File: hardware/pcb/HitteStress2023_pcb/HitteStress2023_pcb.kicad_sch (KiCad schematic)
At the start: 5 parts

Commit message: Update drawing
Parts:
- added J1: Conn_01x02_Socket, Connector_Phoenix_GMSTB:PhoenixContact_GMSTBVA_2,5_2-G-7,62_1x02_P7.62mm_Vertical, symbol Connector:Conn_01x02_Socket
- added J2: Conn_01x02_Socket, my-KiCad-library:TerminalBlock_Phoenix_MPT-0,5-2-2.54_1x02_P2.54mm_Horizontal, symbol Connector:Conn_01x02_Socket
- P1: footprint (none) -> my-KiCad-library:HLK-5M05
- S1: value ~ -> AM2315C; footprint (none) -> my-KiCad-library:AM2315C
- S2: value ~ -> SPS30; footprint (none) -> my-KiCad-library:SPS30
- U1: renamed from U2; value ~ -> MINIDCDCBOOST5V; footprint (none) -> my-KiCad-library:MINIDCDCBOOST5V
- U2: renamed from U1; value ~ -> TTGO_T-Beam_T22_V1.1; footprint (none) -> my-KiCad-library:TTGO_T-Beam_T22_V1.1
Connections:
- net GND: now also P1.3 (-Vo), J2.1 (Pin_1)
- net at P1.1 (AC): now also J1.2 (Pin_2)
- net at P1.2 (AC): now also J1.1 (Pin_1)
- net 5V_I: now reaches P1.4 (+Vo)
- net 5V_I: now also J2.2 (Pin_2)
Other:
- moved on the sheet: U1
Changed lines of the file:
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@@
 (kicad_sch (version 20230121) (generator eeschema)
   (paper "A4")
+  (wire (pts (xy 81.28 64.77) (xy 81.28 66.04))
+    (stroke (width 0) (type default))
+  )
   (wire (pts (xy 177.8 64.77) (xy 193.04 64.77))
     (stroke (width 0) (type default))
   )
+  (wire (pts (xy 81.28 60.96) (xy 81.28 62.23))
+    (stroke (width 0) (type default))
+  )
+  (wire (pts (xy 44.45 66.04) (xy 44.45 64.77))
+    (stroke (width 0) (type default))
+  )
   (wire (pts (xy 177.8 97.79) (xy 193.04 97.79))
     (stroke (width 0) (type default))
@@
     (stroke (width 0) (type default))
   )
+  (wire (pts (xy 86.36 64.77) (xy 81.28 64.77))
+    (stroke (width 0) (type default))
+  )
+  (wire (pts (xy 36.83 62.23) (xy 44.45 62.23))
+    (stroke (width 0) (type default))
+  )
   (wire (pts (xy 105.41 87.63) (xy 120.65 87.63))
     (stroke (width 0) (type default))
   )
-  (wire (pts (xy 78.74 107.95) (xy 99.06 107.95))
+  (wire (pts (xy 72.39 106.68) (xy 92.71 106.68))
     (stroke (width 0) (type default))
   )
@@
     (stroke (width 0) (type default))
   )
-  (wire (pts (xy 87.63 96.52) (xy 99.06 96.52))
+  (wire (pts (xy 81.28 95.25) (xy 92.71 95.25))
+    (stroke (width 0) (type default))
+  )
+  (wire (pts (xy 44.45 62.23) (xy 44.45 60.96))
+    (stroke (width 0) (type default))
+  )
+  (wire (pts (xy 52.07 66.04) (xy 44.45 66.04))
+    (stroke (width 0) (type default))
+  )
+  (wire (pts (xy 81.28 62.23) (xy 86.36 62.23))
     (stroke (width 0) (type default))
   )
@@
     (stroke (width 0) (type default))
   )
-  (wire (pts (xy 58.42 96.52) (xy 69.85 96.52))
+  (wire (pts (xy 52.07 95.25) (xy 63.5 95.25))
     (stroke (width 0) (type default))
   )
@@
     (stroke (width 0) (type default))
   )
-  (wire (pts (xy 78.74 105.41) (xy 78.74 107.95))
+  (wire (pts (xy 74.93 60.96) (xy 81.28 60.96))
+    (stroke (width 0) (type default))
+  )
+  (wire (pts (xy 44.45 64.77) (xy 36.83 64.77))
+    (stroke (width 0) (type default))
+  )
+  (wire (pts (xy 72.39 104.14) (xy 72.39 106.68))
     (stroke (width 0) (type default))
   )
@@
     (stroke (width 0) (type default))
   )
+  (wire (pts (xy 44.45 60.96) (xy 52.07 60.96))
+    (stroke (width 0) (type default))
+  )
   (wire (pts (xy 177.8 95.25) (xy 193.04 95.25))
+    (stroke (width 0) (type default))
+  )
+  (wire (pts (xy 81.28 66.04) (xy 74.93 66.04))
     (stroke (width 0) (type default))
   )
@@
     (effects (font (size 1.27 1.27)) (justify left bottom))
   )
-  (label "GND" (at 97.79 107.95 180) (fields_autoplaced)
+  (label "GND" (at 91.44 106.68 180) (fields_autoplaced)
     (effects (font (size 1.27 1.27)) (justify right bottom))
   )
@@
     (effects (font (size 1.27 1.27)) (justify left bottom))
   )
-  (label "5V_U" (at 59.69 96.52 0) (fields_autoplaced)
+  (label "5V_U" (at 53.34 95.25 0) (fields_autoplaced)
+    (effects (font (size 1.27 1.27)) (justify left bottom))
+  )
+  (label "GND" (at 76.2 66.04 0) (fields_autoplaced)
     (effects (font (size 1.27 1.27)) (justify left bottom))
   )
@@
     (effects (font (size 1.27 1.27)) (justify left bottom))
   )
-  (label "5V_SPS" (at 97.79 96.52 180) (fields_autoplaced)
+  (label "5V_SPS" (at 91.44 95.25 180) (fields_autoplaced)
     (effects (font (size 1.27 1.27)) (justify right bottom))
   )
@@
     (effects (font (size 1.27 1.27)) (justify left bottom))
   )
+  (label "5V_I" (at 76.2 60.96 0) (fields_autoplaced)
+    (effects (font (size 1.27 1.27)) (justify left bottom))
+  )
   (label "GND" (at 106.68 77.47 0) (fields_autoplaced)
     (effects (font (size 1.27 1.27)) (justify left bottom))
@@
   (symbol (lib_id "my-KiCad-library:TTGO_T-Beam_T22_V1.1") (at 135.89 80.01 0) (unit 1)
     (in_bom yes) (on_board yes) (dnp no) (fields_autoplaced)
-    (property "Reference" "U1" (at 135.89 55.88 0)
-      (effects (font (size 1.27 1.27)))
-    )
-    (property "Value" "~" (at 135.89 80.01 0)
-      (effects (font (size 1.27 1.27)))
-    )
-    (property "Footprint" "" (at 135.89 80.01 0)
+    (property "Reference" "U2" (at 135.89 55.88 0)
+      (effects (font (size 1.27 1.27)))
+    )
+    (property "Value" "TTGO_T-Beam_T22_V1.1" (at 135.89 80.01 0)
+      (effects (font (size 1.27 1.27)))
+    )
+    (property "Footprint" "my-KiCad-library:TTGO_T-Beam_T22_V1.1" (at 135.89 80.01 0)
       (effects (font (size 1.27 1.27)) hide)
     )
@@
       (project "HitteStress2023_pcb"
         (path "/0b1ba7fb-a496-4717-8ed8-2a7de64e001c"
+          (reference "U2") (unit 1)
+        )
+      )
+    )
+  )
+  (symbol (lib_id "my-KiCad-library:MINIDCDCBOOST5V") (at 72.39 95.25 0) (unit 1)
+    (in_bom yes) (on_board yes) (dnp no) (fields_autoplaced)
+    (property "Reference" "U1" (at 74.91 83.82 0)
+      (effects (font (size 1.27 1.27)))
+    )
+    (property "Value" "MINIDCDCBOOST5V" (at 72.39 95.25 0)
+      (effects (font (size 1.27 1.27)))
+    )
+    (property "Footprint" "my-KiCad-library:MINIDCDCBOOST5V" (at 72.39 95.25 0)
+      (effects (font (size 1.27 1.27)) hide)
+    )
+    (property "Datasheet" "https://www.tinytronics.nl/shop/nl/power/spanningsconverters/boost-(step-up)-converters/mini-dc-dc-5v-step-up-boost-converter-480ma" (at 72.39 118.11 0)
+      (effects (font (size 1.27 1.27)) hide)
+    )
+    (pin "2")
+    (pin "3")
+    (pin "1")
+    (instances
+      (project "HitteStress2023_pcb"
+        (path "/0b1ba7fb-a496-4717-8ed8-2a7de64e001c"
           (reference "U1") (unit 1)
-        )
-      )
-    )
-  )
-  (symbol (lib_id "my-KiCad-library:MINIDCDCBOOST5V") (at 78.74 96.52 0) (unit 1)
-    (in_bom yes) (on_board yes) (dnp no) (fields_autoplaced)
-    (property "Reference" "U2" (at 81.26 85.09 0)
-      (effects (font (size 1.27 1.27)))
-    )
-    (property "Value" "~" (at 78.74 96.52 0)
-      (effects (font (size 1.27 1.27)))
-    )
-    (property "Footprint" "" (at 78.74 96.52 0)
-      (effects (font (size 1.27 1.27)) hide)
-    )
-    (property "Datasheet" "https://www.tinytronics.nl/shop/nl/power/spanningsconverters/boost-(step-up)-converters/mini-dc-dc-5v-step-up-boost-converter-480ma" (at 78.74 119.38 0)
-      (effects (font (size 1.27 1.27)) hide)
-    )
-    (pin "2")
-    (pin "3")
-    (pin "1")
-    (instances
-      (project "HitteStress2023_pcb"
-        (path "/0b1ba7fb-a496-4717-8ed8-2a7de64e001c"
-          (reference "U2") (unit 1)
         )
       )
@@
       (effects (font (size 1.27 1.27)) (justify left))
     )
-    (property "Value" "~" (at 199.39 68.58 0)
-      (effects (font (size 1.27 1.27)))
-    )
-    (property "Footprint" "" (at 199.39 68.58 0)
+    (property "Value" "AM2315C" (at 199.39 68.58 0)
+      (effects (font (size 1.27 1.27)))
+    )
+    (property "Footprint" "my-KiCad-library:AM2315C" (at 199.39 68.58 0)
       (effects (font (size 1.27 1.27)) hide)
     )
@@
       (effects (font (size 1.27 1.27)) (justify left))
     )
-    (property "Value" "~" (at 203.2 100.33 0)
-      (effects (font (size 1.27 1.27)))
-    )
-    (property "Footprint" "" (at 203.2 100.33 0)
+    (property "Value" "SPS30" (at 203.2 100.33 0)
+      (effects (font (size 1.27 1.27)))
+    )
+    (property "Footprint" "my-KiCad-library:SPS30" (at 203.2 100.33 0)
       (effects (font (size 1.27 1.27)) hide)
     )
@@
     )
   )
+  (symbol (lib_id "Connector:Conn_01x02_Socket") (at 31.75 64.77 180) (unit 1)
+    (in_bom yes) (on_board yes) (dnp no) (fields_autoplaced)
+    (property "Reference" "J1" (at 32.385 57.15 0)
+      (effects (font (size 1.27 1.27)))
+    )
+    (property "Value" "Conn_01x02_Socket" (at 32.385 59.69 0)
+      (effects (font (size 1.27 1.27)))
+    )
+    (property "Footprint" "Connector_Phoenix_GMSTB:PhoenixContact_GMSTBVA_2,5_2-G-7,62_1x02_P7.62mm_Vertical" (at 31.75 64.77 0)
+      (effects (font (size 1.27 1.27)) hide)
+    )
+    (property "Datasheet" "~" (at 31.75 64.77 0)
+      (effects (font (size 1.27 1.27)) hide)
+    )
+    (pin "1")
+    (pin "2")
+    (instances
+      (project "HitteStress2023_pcb"
+        (path "/0b1ba7fb-a496-4717-8ed8-2a7de64e001c"
+          (reference "J1") (unit 1)
+        )
+      )
+    )
+  )
+  (symbol (lib_id "Connector:Conn_01x02_Socket") (at 91.44 64.77 0) (mirror x) (unit 1)
+    (in_bom yes) (on_board yes) (dnp no)
+    (property "Reference" "J2" (at 92.71 64.77 0)
+      (effects (font (size 1.27 1.27)) (justify left))
+    )
+    (property "Value" "Conn_01x02_Socket" (at 92.71 62.23 0)
+      (effects (font (size 1.27 1.27)) (justify left))
+    )
+    (property "Footprint" "my-KiCad-library:TerminalBlock_Phoenix_MPT-0,5-2-2.54_1x02_P2.54mm_Horizontal" (at 91.44 64.77 0)
+      (effects (font (size 1.27 1.27)) hide)
+    )
+    (property "Datasheet" "~" (at 91.44 64.77 0)
+      (effects (font (size 1.27 1.27)) hide)
+    )
+    (pin "1")
+    (pin "2")
+    (instances
+      (project "HitteStress2023_pcb"
+        (path "/0b1ba7fb-a496-4717-8ed8-2a7de64e001c"
+          (reference "J2") (unit 1)
+        )
+      )
+    )
+  )
   (symbol (lib_id "my-KiCad-library:HLK-5M05") (at 63.5 63.5 0) (unit 1)
     (in_bom yes) (on_board yes) (dnp no) (fields_autoplaced)
@@
       (effects (font (size 1.27 1.27)))
     )
-    (property "Footprint" "" (at 63.5 63.5 0)
-      (effects (font (size 1.27 1.27)) hide)
-    )
+    (property "Footprint" "my-KiCad-library:HLK-5M05" (at 63.5 63.5 0)
+      (effects (font (size 1.27 1.27)) hide)
+    )

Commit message: Finalised the day
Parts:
- added J3: SMA_conector_female, my-KiCad-library:SMA-ANT-CONN, symbol Connector:Conn_01x01_Pin
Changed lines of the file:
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@@
+    )
+  )
+  (symbol (lib_id "Connector:Conn_01x01_Pin") (at 44.45 152.4 0) (unit 1)
+    (in_bom yes) (on_board yes) (dnp no) (fields_autoplaced)
+    (property "Reference" "J3" (at 45.085 147.32 0)
+      (effects (font (size 1.27 1.27)))
+    )
+    (property "Value" "SMA_conector_female" (at 45.085 149.86 0)
+      (effects (font (size 1.27 1.27)))
+    )
+    (property "Footprint" "my-KiCad-library:SMA-ANT-CONN" (at 44.45 152.4 0)
+      (effects (font (size 1.27 1.27)) hide)
+    )
+    (property "Datasheet" "~" (at 44.45 152.4 0)
+      (effects (font (size 1.27 1.27)) hide)
+    )
+    (pin "1")
+    (instances
+      (project "HitteStress2023_pcb"
+        (path "/0b1ba7fb-a496-4717-8ed8-2a7de64e001c"
+          (reference "J3") (unit 1)
+        )
+      )
     )
   )

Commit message: Updates
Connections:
- net GND: now also J3.1 (Pin_1)
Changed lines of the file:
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@@
+    (stroke (width 0) (type default))
+  )
+  (wire (pts (xy 49.53 152.4) (xy 67.31 152.4))
     (stroke (width 0) (type default))
   )
@@
     (effects (font (size 1.27 1.27)) (justify left bottom))
   )
+  (label "GND" (at 59.69 152.4 0) (fields_autoplaced)
+    (effects (font (size 1.27 1.27)) (justify left bottom))
+  )

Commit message: Verified and updated to v0.9 for first prototype print and ordered it.
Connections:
- net 3V3: now also U2.16 (3V3); no longer U2.20 (3V3)
- net GND: now also S2.4 (SEL)
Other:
- company: (none) -> IoT-Apeldoorn
- title: (none) -> Ittestress 2023 (Homerus Edition)
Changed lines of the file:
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@@
 (kicad_sch (version 20230121) (generator eeschema)
   (paper "A4")
+  (title_block
+    (title "Ittestress 2023 (Homerus Edition)")
+    (date "2024-01-01")
+    (rev "0.9")
+    (company "IoT-Apeldoorn")
+    (comment 1 "Designed by RFSee for")
+    (comment 2 "https://github.com/TTNApeldoorn/aid-hittestress-2023")
+  )
+  (junction (at 188.214 105.41) (diameter 0) (color 0 0 0 0)
+  )
   (wire (pts (xy 81.28 64.77) (xy 81.28 66.04))
+    (stroke (width 0) (type default))
+  )
+  (wire (pts (xy 193.04 102.87) (xy 188.214 102.87))
     (stroke (width 0) (type default))
   )
@@
     (stroke (width 0) (type default))
   )
+  (wire (pts (xy 188.214 105.41) (xy 177.8 105.41))
+    (stroke (width 0) (type default))
+  )
   (wire (pts (xy 72.39 106.68) (xy 92.71 106.68))
     (stroke (width 0) (type default))
@@
     (stroke (width 0) (type default))
   )
-  (wire (pts (xy 193.04 105.41) (xy 177.8 105.41))
+  (wire (pts (xy 193.04 105.41) (xy 188.214 105.41))
     (stroke (width 0) (type default))
   )
-  (wire (pts (xy 105.41 80.01) (xy 120.65 80.01))
+  (wire (pts (xy 105.41 90.17) (xy 120.65 90.17))
     (stroke (width 0) (type default))
   )
@@
   )
   (wire (pts (xy 74.93 60.96) (xy 81.28 60.96))
+    (stroke (width 0) (type default))
+  )
+  (wire (pts (xy 188.214 102.87) (xy 188.214 105.41))
     (stroke (width 0) (type default))
   )
@@
     (effects (font (size 1.27 1.27)) (justify left bottom))
   )
-  (label "3V3" (at 106.68 80.01 0) (fields_autoplaced)
+  (label "3V3" (at 106.68 90.17 0) (fields_autoplaced)
     (effects (font (size 1.27 1.27)) (justify left bottom))
   )

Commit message: Version 1.0 after prototype soldering
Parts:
- J1: footprint Connector_Phoenix_GMSTB:PhoenixContact_GMSTBVA_2,5_2-G-7,62_1x02_P7.62mm_Vertical -> Connector_Phoenix_MC_HighVoltage:PhoenixContact_MCV_1,5_2-G-5.08_1x02_P5.08mm_Vertical
- J2: footprint my-KiCad-library:TerminalBlock_Phoenix_MPT-0,5-2-2.54_1x02_P2.54mm_Horizontal -> TerminalBlock_Phoenix:TerminalBlock_Phoenix_MPT-0,5-2-2.54_1x02_P2.54mm_Horizontal
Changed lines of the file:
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@@
   (title_block
     (title "Ittestress 2023 (Homerus Edition)")
-    (date "2024-01-01")
-    (rev "0.9")
+    (date "2024-01-08")
+    (rev "1.0")
     (company "IoT-Apeldoorn")
     (comment 1 "Designed by RFSee for")
@@
       (effects (font (size 1.27 1.27)))
     )
-    (property "Footprint" "Connector_Phoenix_GMSTB:PhoenixContact_GMSTBVA_2,5_2-G-7,62_1x02_P7.62mm_Vertical" (at 31.75 64.77 0)
+    (property "Footprint" "Connector_Phoenix_MC_HighVoltage:PhoenixContact_MCV_1,5_2-G-5.08_1x02_P5.08mm_Vertical" (at 31.75 64.77 0)
       (effects (font (size 1.27 1.27)) hide)
     )
@@
       (effects (font (size 1.27 1.27)) (justify left))
     )
-    (property "Footprint" "my-KiCad-library:TerminalBlock_Phoenix_MPT-0,5-2-2.54_1x02_P2.54mm_Horizontal" (at 91.44 64.77 0)
-      (effects (font (size 1.27 1.27)) hide)
-    )
+    (property "Footprint" "TerminalBlock_Phoenix:TerminalBlock_Phoenix_MPT-0,5-2-2.54_1x02_P2.54mm_Horizontal" (at 91.44 64.77 0)
+      (effects (font (size 1.27 1.27)) hide)
+    )

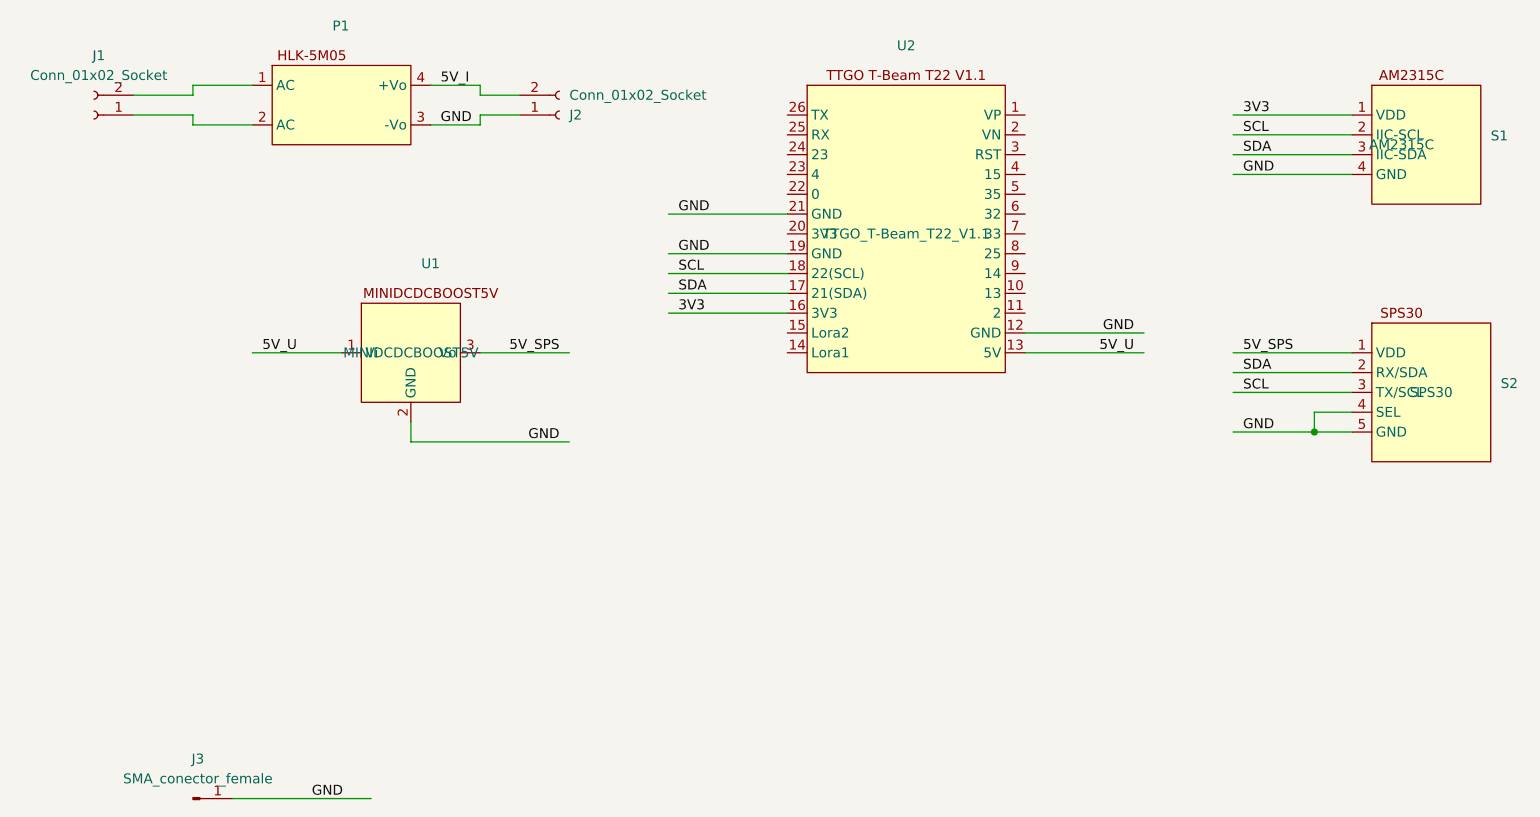
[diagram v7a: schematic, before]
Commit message: Added 2x pull-pup resistors for I2C
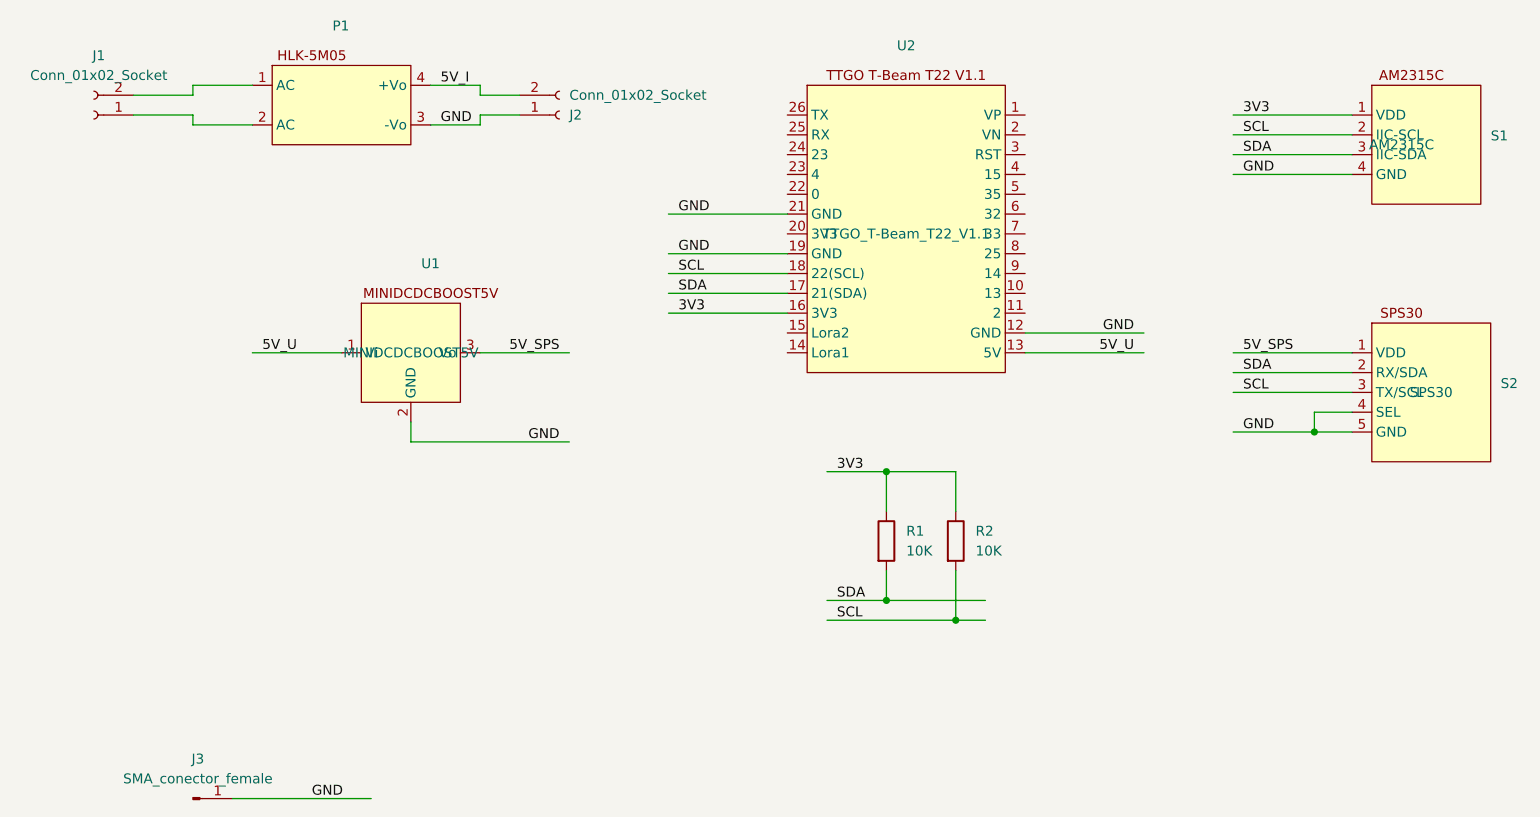
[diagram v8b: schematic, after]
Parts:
- added R1, R2: 10K, Resistor_THT:R_Axial_DIN0309_L9.0mm_D3.2mm_P12.70mm_Horizontal, symbol Device:R
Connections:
- net 3V3: now also R1.1, R2.1
- net SCL: now also R2.2
- net SDA: now also R1.2
